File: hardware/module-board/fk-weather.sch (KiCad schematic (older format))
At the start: 66 parts, among them J1 MICRO-USB, J10 Conn_01x06, J11 Conn_01x06, J3 Conn_01x10, J6 CONN-HDR-2x5, M1 MOUNT_HOLE, M2 MOUNT_HOLE, M3 MOUNT_HOLE, M4 MOUNT_HOLE, Q1 2N7002LT1G, Q2 2N7002LT1G, Q3 2N7002LT1G, Q4 2N7002LT1G, SW1 SPNO, U1 ATSAMD21G18A-AU, U2 MCP1700T-XXX2E, U4 S25FL1xxK0XM, Y1 FC-135

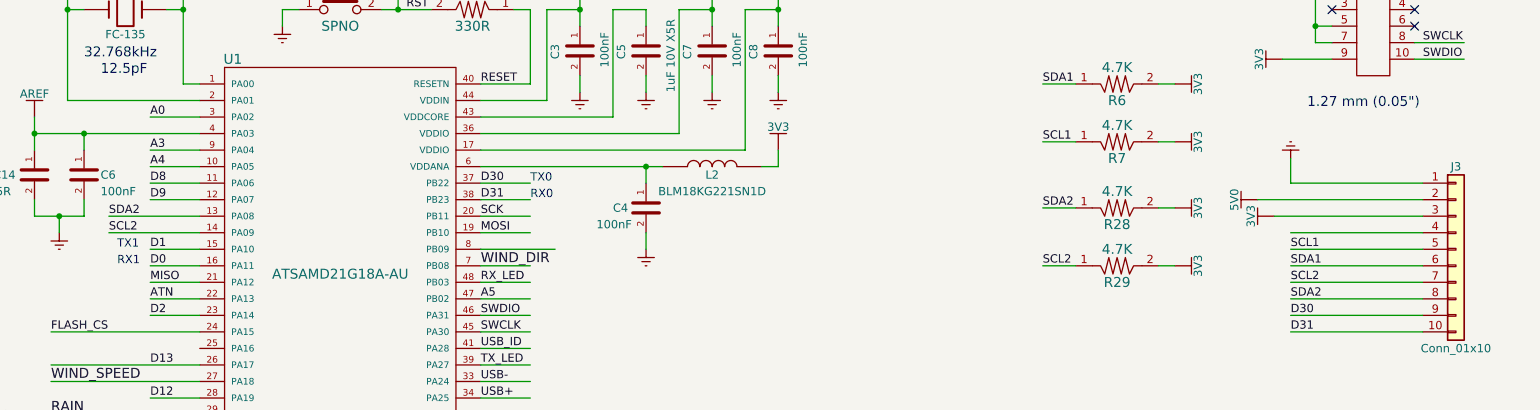
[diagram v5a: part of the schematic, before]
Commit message: Change header orien. Plot.
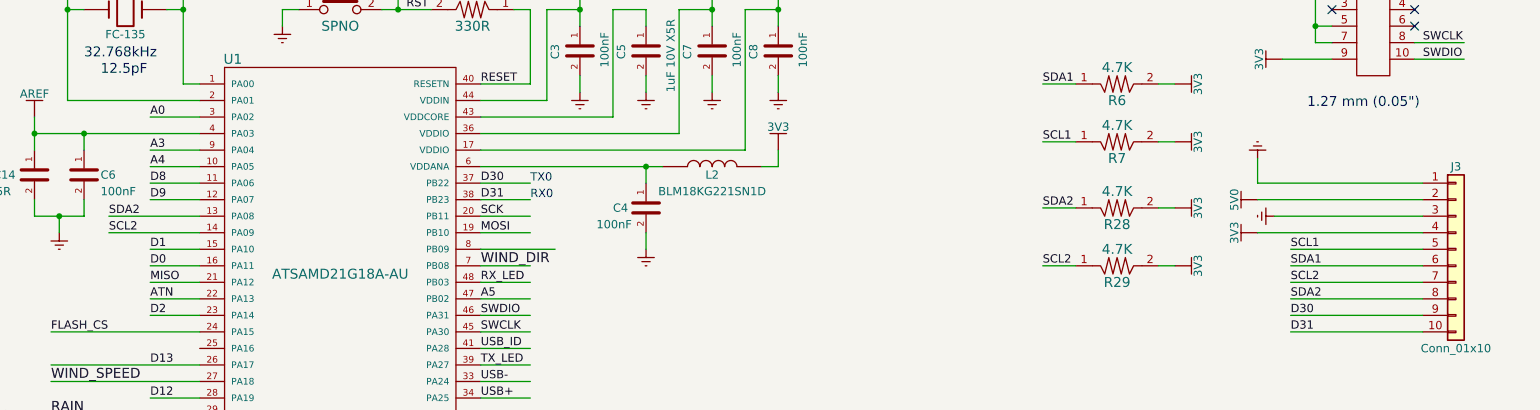
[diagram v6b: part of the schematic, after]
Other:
- note removed: "RX1"
- note removed: "TX1"
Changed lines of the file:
@@
 L 3V3 #PWR017
 U 1 1 5977AC6E
-P 9150 2750
-F 0 "#PWR017" H 9150 2600 50  0001 C CNN
-F 1 "3V3" H 9150 2890 50  0000 C CNN
-F 2 "" H 9150 2750 60  0000 C CNN
-F 3 "" H 9150 2750 60  0000 C CNN
-	1    9150 2750
+P 9050 2850
+F 0 "#PWR017" H 9050 2700 50  0001 C CNN
+F 1 "3V3" H 9050 2990 50  0000 C CNN
+F 2 "" H 9050 2850 60  0000 C CNN
+F 3 "" H 9050 2850 60  0000 C CNN
+	1    9050 2850
 	0    -1   -1   0
 $EndComp
@@
 L GND #PWR018
 U 1 1 5977ACB8
-P 9250 2400
-F 0 "#PWR018" H 9250 2150 50  0001 C CNN
-F 1 "GND" H 9250 2250 50  0001 C CNN
-F 2 "" H 9250 2400 60  0000 C CNN
-F 3 "" H 9250 2400 60  0000 C CNN
-	1    9250 2400
+P 9050 2400
+F 0 "#PWR018" H 9050 2150 50  0001 C CNN
+F 1 "GND" H 9050 2250 50  0001 C CNN
+F 2 "" H 9050 2400 60  0000 C CNN
+F 3 "" H 9050 2400 60  0000 C CNN
+	1    9050 2400
 	-1   0    0    1
 $EndComp
@@
 Text Notes 4650 2650 0    50   ~ 0
 RX0
-Text Notes 2150 3050 0    50   ~ 0
-RX1
-Text Notes 2150 2950 0    50   ~ 0
-TX1
 Text Notes 1100 4300 0    60   ~ 0
 M2.5 size
@@
 	4350 2450 5450 2450
 Wire Wire Line
-	9250 2850 10050 2850
+	9050 2850 10050 2850
 Wire Wire Line
 	9250 2950 10050 2950
@@
 	9150 2750 10050 2750
 Wire Wire Line
-	9250 2550 10050 2550
-Wire Wire Line
-	9250 2400 9250 2550
+	9050 2550 10050 2550
+Wire Wire Line
+	9050 2400 9050 2550
 Wire Wire Line
 	9050 2650 10050 2650
@@
 Wire Wire Line
 	9250 3450 10050 3450
+$Comp
+L GND #PWR051
+U 1 1 5A45CD21
+P 9150 2750
+F 0 "#PWR051" H 9150 2500 50  0001 C CNN
+F 1 "GND" H 9150 2600 50  0001 C CNN
+F 2 "" H 9150 2750 60  0000 C CNN
+F 3 "" H 9150 2750 60  0000 C CNN
+	1    9150 2750
+	0    1    1    0
+$EndComp
 $EndSCHEMATC

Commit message: Using the prettier footprints for some passives.
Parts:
- C1, C10, C11, C12, C14, C18, C2, C3, C4, C5, C6, C7, C8, C9: footprint Capacitors_SMD:C_0603_HandSoldering -> RocketScreamKicadLibrary:CAP-0603
- L1, L2: footprint Inductors_SMD:L_0603_HandSoldering -> RocketScreamKicadLibrary:IND-0603
- R1, R10, R17, R2, R22, R23, R28, R29, R3, R30, R31, R32, R33, R34, R4, R5, R6, R7, R8, R9: footprint Resistors_SMD:R_0603_HandSoldering -> RocketScreamKicadLibrary:RES-0603

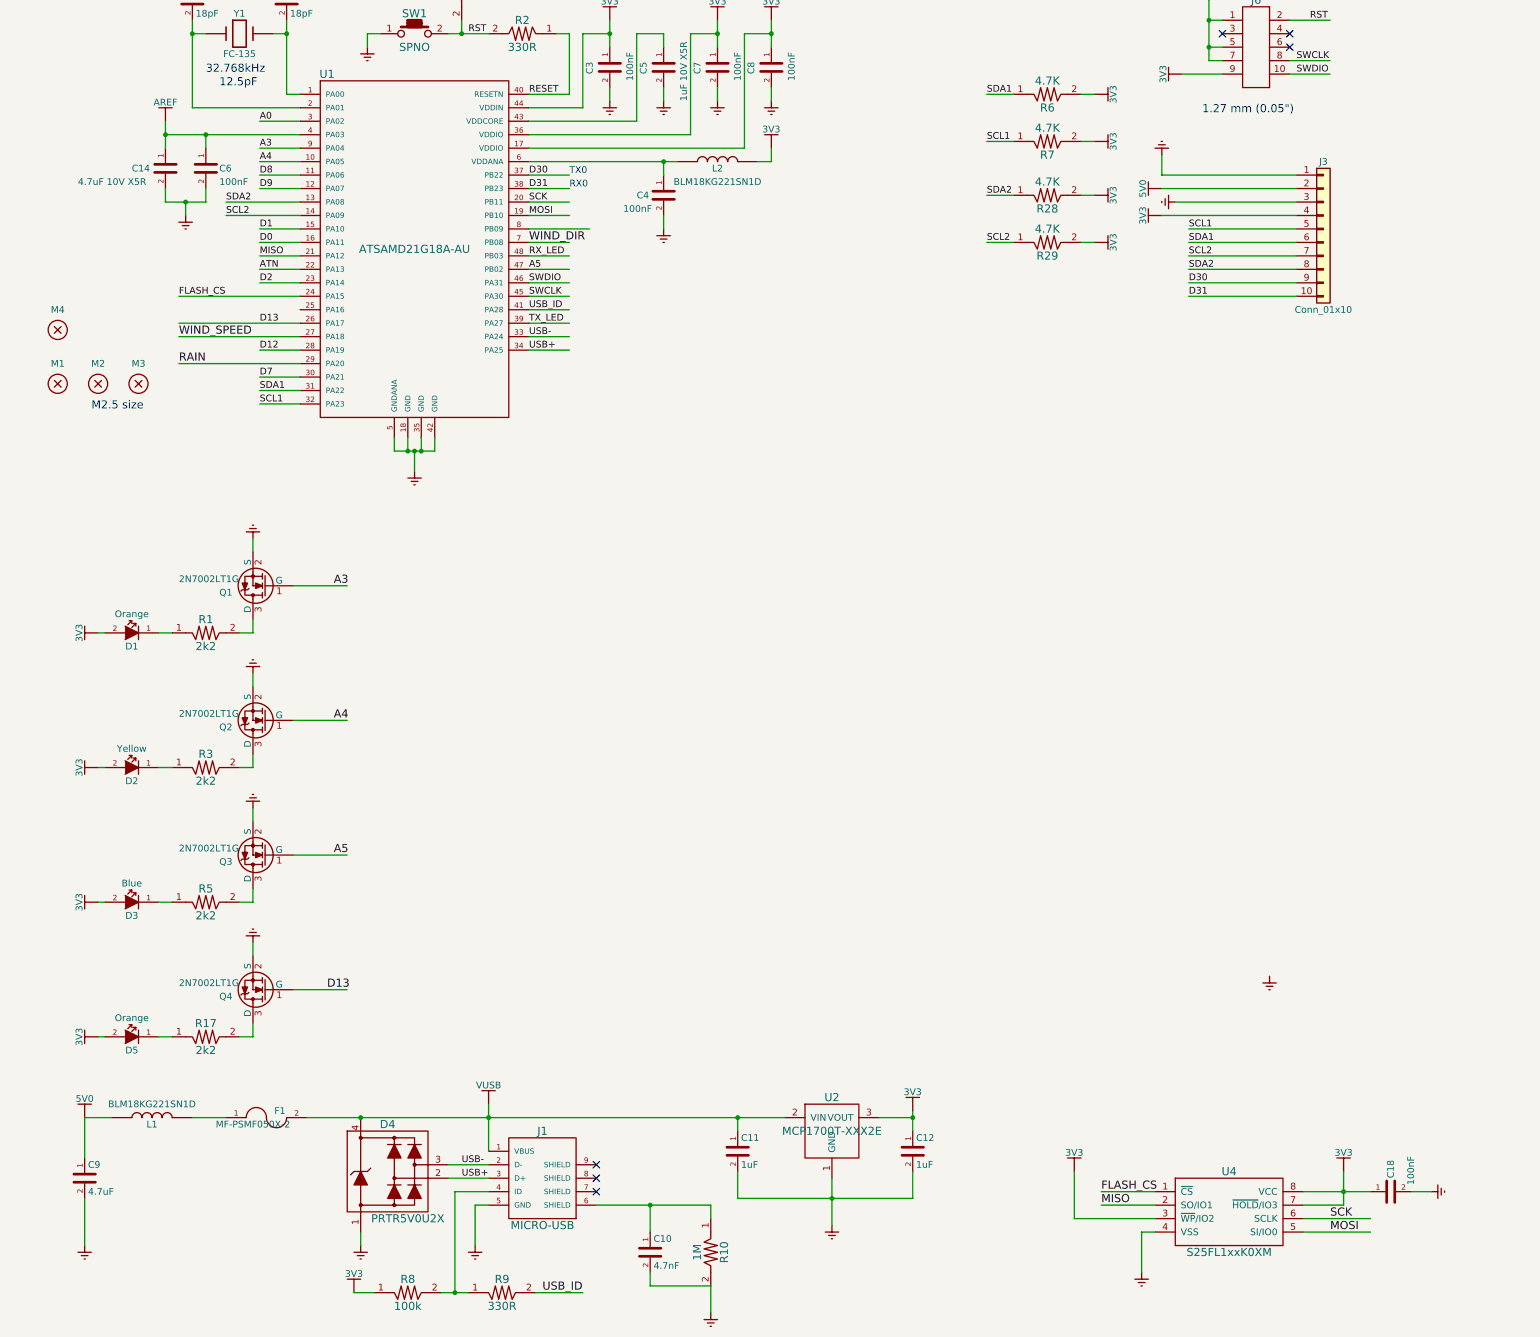
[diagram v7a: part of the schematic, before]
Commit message: Add NFET for peripherals. In this case just the flash.
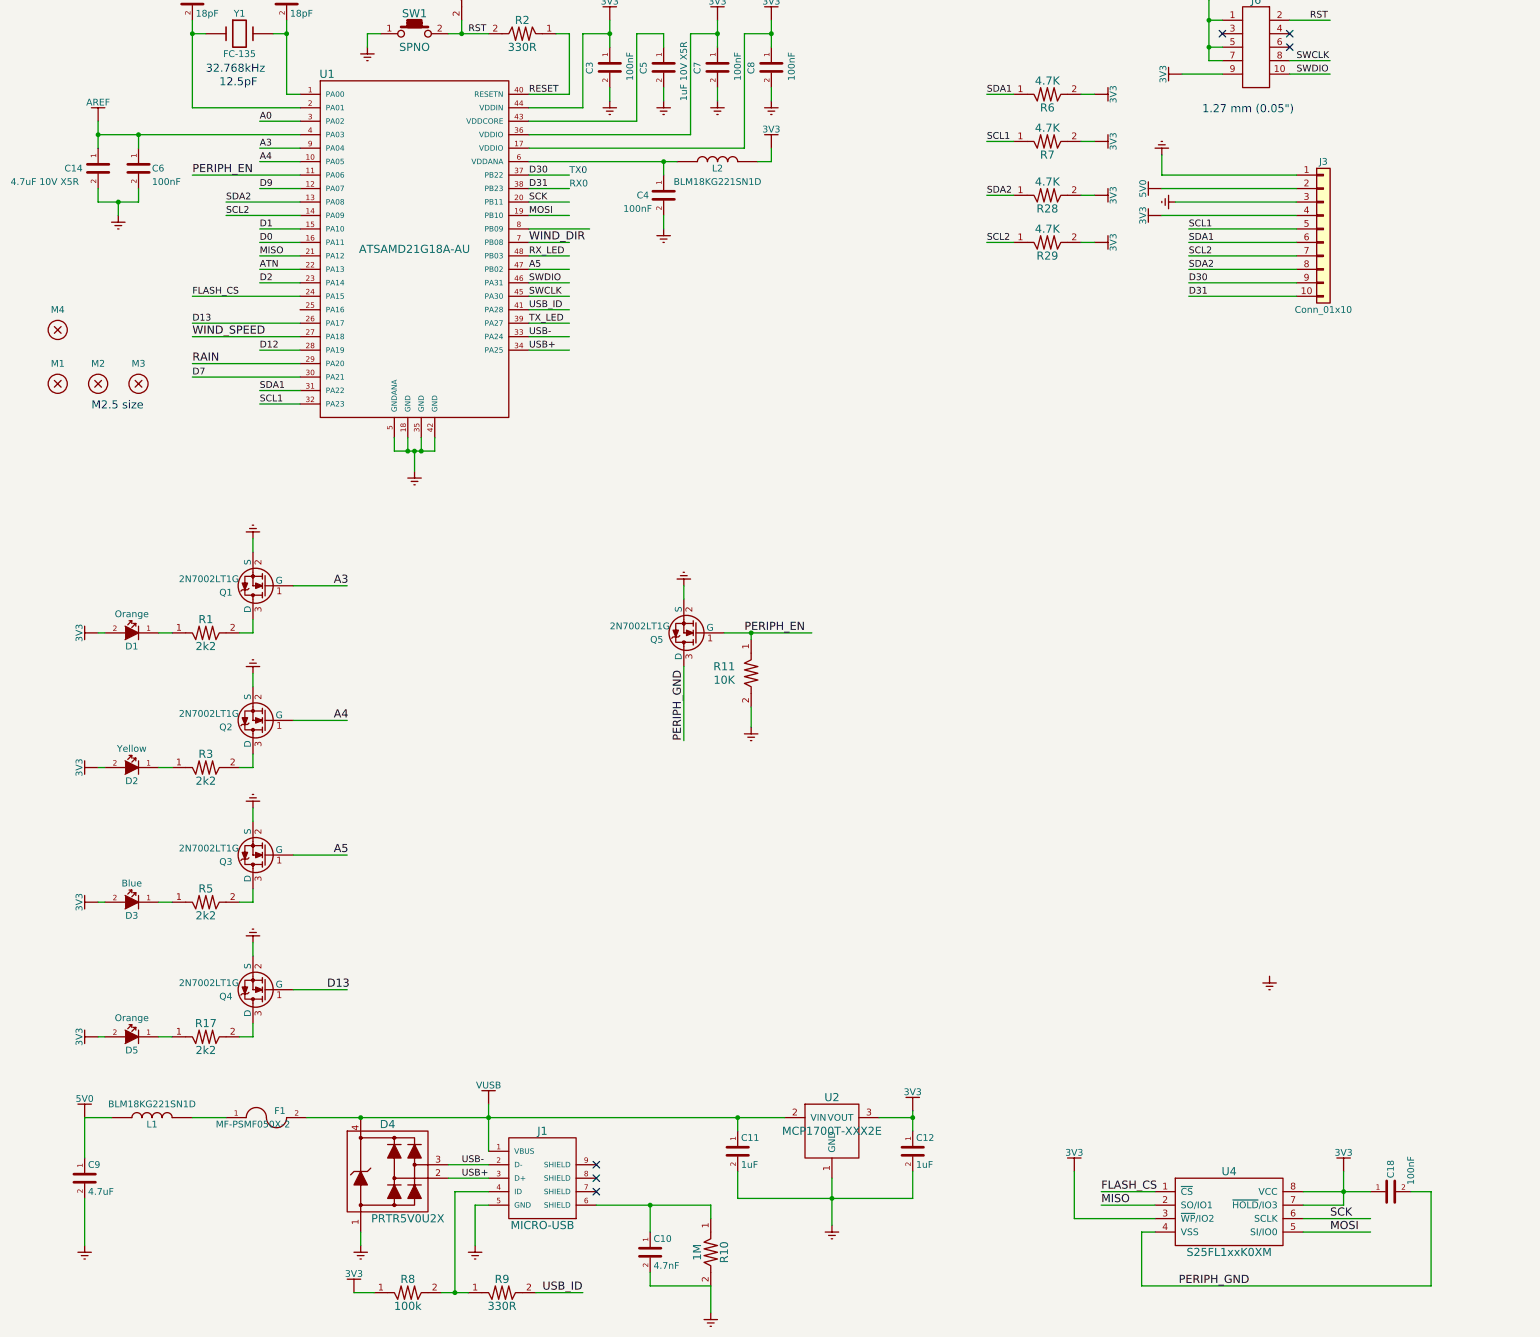
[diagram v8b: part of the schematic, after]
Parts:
- added Q5: 2N7002LT1G, RocketScreamKicadLibrary:SOT-23, symbol MOSFET-N
- added R11: 10K, RocketScreamKicadLibrary:RES-0603, symbol RESISTOR
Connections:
- net labels added: PERIPH_EN, PERIPH_GND
- net labels removed: D8
- wire segments 216 -> 223
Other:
- moved on the sheet: C14, C6
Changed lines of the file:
@@
 L AREF #PWR013
 U 1 1 56101489
-P 1650 2150
-F 0 "#PWR013" H 1650 2000 50  0001 C CNN
-F 1 "AREF" H 1650 2290 50  0000 C CNN
-F 2 "" H 1650 2150 60  0000 C CNN
-F 3 "" H 1650 2150 60  0000 C CNN
-	1    1650 2150
+P 1150 2150
+F 0 "#PWR013" H 1150 2000 50  0001 C CNN
+F 1 "AREF" H 1150 2290 50  0000 C CNN
+F 2 "" H 1150 2150 60  0000 C CNN
+F 3 "" H 1150 2150 60  0000 C CNN
+	1    1150 2150
 	1    0    0    -1
 $EndComp
@@
 L CAPACITOR-CERAMIC C6
 U 1 1 56101EA7
-P 1950 2500
-F 0 "C6" H 2050 2500 50  0000 L CNN
-F 1 "100nF" H 2050 2400 50  0000 L CNN
-F 2 "RocketScreamKicadLibrary:CAP-0603" H 1950 2300 30  0001 C CNN
-F 3 "" H 1950 2500 60  0000 C CNN
-F 4 "0" H 2050 2600 50  0001 C CNN "price"
-F 5 "81-GRM39X104K50D" H -200 -150 50  0001 C CNN "spn1"
-F 6 "mouser" H -200 -150 50  0001 C CNN "supplier1"
-	1    1950 2500
+P 1450 2500
+F 0 "C6" H 1550 2500 50  0000 L CNN
+F 1 "100nF" H 1550 2400 50  0000 L CNN
+F 2 "RocketScreamKicadLibrary:CAP-0603" H 1450 2300 30  0001 C CNN
+F 3 "" H 1450 2500 60  0000 C CNN
+F 4 "0" H 1550 2600 50  0001 C CNN "price"
+F 5 "81-GRM39X104K50D" H -700 -150 50  0001 C CNN "spn1"
+F 6 "mouser" H -700 -150 50  0001 C CNN "supplier1"
+	1    1450 2500
 	1    0    0    -1
 $EndComp
@@
 L CAPACITOR-CERAMIC C14
 U 1 1 561023B1
-P 1650 2500
-F 0 "C14" H 1400 2500 50  0000 L CNN
-F 1 "4.7uF 10V X5R" H 1000 2400 50  0000 L CNN
-F 2 "RocketScreamKicadLibrary:CAP-0603" H 1650 2300 30  0001 C CNN
-F 3 "" H 1650 2500 60  0000 C CNN
-F 4 "0" H 1400 2600 50  0001 C CNN "price"
-F 5 "581-0603ZD475MAT2A" H -200 -150 50  0001 C CNN "spn1"
-F 6 "mouser" H -200 -150 50  0001 C CNN "supplier1"
-	1    1650 2500
+P 1150 2500
+F 0 "C14" H 900 2500 50  0000 L CNN
+F 1 "4.7uF 10V X5R" H 500 2400 50  0000 L CNN
+F 2 "RocketScreamKicadLibrary:CAP-0603" H 1150 2300 30  0001 C CNN
+F 3 "" H 1150 2500 60  0000 C CNN
+F 4 "0" H 900 2600 50  0001 C CNN "price"
+F 5 "581-0603ZD475MAT2A" H -700 -150 50  0001 C CNN "spn1"
+F 6 "mouser" H -700 -150 50  0001 C CNN "supplier1"
+	1    1150 2500
 	1    0    0    -1
 $EndComp
@@
 L GND #PWR014
 U 1 1 5610322B
-P 1800 2850
-F 0 "#PWR014" H 1800 2600 50  0001 C CNN
-F 1 "GND" H 1800 2700 50  0001 C CNN
-F 2 "" H 1800 2850 60  0000 C CNN
-F 3 "" H 1800 2850 60  0000 C CNN
-	1    1800 2850
+P 1300 2850
+F 0 "#PWR014" H 1300 2600 50  0001 C CNN
+F 1 "GND" H 1300 2700 50  0001 C CNN
+F 2 "" H 1300 2850 60  0000 C CNN
+F 3 "" H 1300 2850 60  0000 C CNN
+	1    1300 2850
 	1    0    0    -1
 $EndComp
@@
 Text Label 2350 2450 0    50   ~ 0
 A4
-Text Label 2350 2550 0    50   ~ 0
-D8
 Text Label 2350 2650 0    50   ~ 0
 D9
@@
 Text Label 2350 3350 0    50   ~ 0
 D2
-Text Label 1750 3450 0    50   ~ 0
+Text Label 1850 3450 0    50   ~ 0
 FLASH_CS
 Text Label 2350 3850 0    50   ~ 0
 D12
-Text Label 2350 4050 0    50   ~ 0
-D7
 Text Label 2350 4150 0    50   ~ 0
 SDA1
@@
 Text Label 2850 8600 0    60   ~ 0
 D13
-Text Label 2350 3650 0    50   ~ 0
+Text Label 1850 3650 0    50   ~ 0
 D13
 Text Label 2100 2750 0    50   ~ 0
@@
 $EndComp
 $Comp
-L GND #PWR045
-U 1 1 5A1CDAB1
-P 11050 10100
-F 0 "#PWR045" H 11050 9850 50  0001 C CNN
-F 1 "GND" H 11050 9950 50  0001 C CNN
-F 2 "" H 11050 10100 60  0000 C CNN
-F 3 "" H 11050 10100 60  0000 C CNN
-	1    11050 10100
-	0    -1   -1   0
-$EndComp
-$Comp
 L Conn_01x06 J11
 U 1 1 5A44A535
@@
 	2650 2150 2350 2150
 Wire Wire Line
-	1650 2250 2650 2250
+	1150 2250 2650 2250
 Wire Wire Line
 	2650 2350 2350 2350
@@
 	2650 2450 2350 2450
 Wire Wire Line
-	2650 2550 2350 2550
+	1850 2550 2650 2550
 Wire Wire Line
 	2650 2650 2350 2650
@@
 	2650 3350 2350 3350
 Wire Wire Line
-	1750 3450 2650 3450
-Wire Wire Line
-	1750 3750 2650 3750
+	1850 3450 2650 3450
+Wire Wire Line
+	1850 3750 2650 3750
 Wire Wire Line
 	2650 3850 2350 3850
 Wire Wire Line
-	1750 3950 2650 3950
-Wire Wire Line
-	2650 4050 2350 4050
+	1850 3950 2650 3950
+Wire Wire Line
+	1850 4050 2650 4050
 Wire Wire Line
 	2650 4150 2350 4150
@@
 	1650 1000 1650 1100
 Wire Wire Line
-	1650 2150 1650 2350
-Wire Wire Line
 	4350 3850 4650 3850
 Wire Wire Line
@@
 	3850 800  3850 900
 Wire Wire Line
-	1950 2350 1950 2250
-Wire Wire Line
-	1650 2650 1650 2750
-Wire Wire Line
-	1650 2750 1950 2750
-Wire Wire Line
-	1950 2750 1950 2650
-Wire Wire Line
-	1800 2850 1800 2750
+	1150 2650 1150 2750
+Wire Wire Line
+	1150 2750 1450 2750
+Wire Wire Line
+	1450 2750 1450 2650
+Wire Wire Line
+	1300 2850 1300 2750
 Wire Wire Line
 	9400 1600 9500 1600
@@
 Connection ~ 5350 2450
 Connection ~ 3850 1500
-Connection ~ 1650 2250
-Connection ~ 1950 2250
-Connection ~ 1800 2750
+Connection ~ 1300 2750
 Connection ~ 9400 1600
 Connection ~ 3800 10850
@@
 	9000 10400 8900 10400
 Wire Wire Line
-	8900 10400 8900 10700
+	8900 10400 8900 10800
 Wire Wire Line
 	11050 10100 10900 10100
@@
 Connection ~ 14050 6350
 $Comp
-L 3V3 #PWR046
+L 3V3 #PWR045
 U 1 1 5A4678F1
 P 14500 4700
-F 0 "#PWR046" H 14500 4550 50  0001 C CNN
+F 0 "#PWR045" H 14500 4550 50  0001 C CNN
 F 1 "3V3" H 14500 4840 50  0000 C CNN
 F 2 "" H 14500 4700 60  0000 C CNN
@@
 Connection ~ 14500 4700
 $Comp
-L GND #PWR047
+L GND #PWR046
 U 1 1 5A46880E
 P 14600 6450
-F 0 "#PWR047" H 14600 6200 50  0001 C CNN
+F 0 "#PWR046" H 14600 6200 50  0001 C CNN
 F 1 "GND" H 14600 6300 50  0001 C CNN
 F 2 "" H 14600 6450 60  0000 C CNN
@@
 	14150 1850 14150 1750
 $Comp
-L 3V3 #PWR048
+L 3V3 #PWR047
 U 1 1 5A4762A6
 P 14150 1750
-F 0 "#PWR048" H 14150 1600 50  0001 C CNN
+F 0 "#PWR047" H 14150 1600 50  0001 C CNN
 F 1 "3V3" H 14150 1890 50  0000 C CNN
 F 2 "" H 14150 1750 60  0000 C CNN
@@
 $EndComp
 $Comp
-L GND #PWR049
+L GND #PWR048
 U 1 1 5A476B99
 P 14200 3350
-F 0 "#PWR049" H 14200 3100 50  0001 C CNN
+F 0 "#PWR048" H 14200 3100 50  0001 C CNN
 F 1 "GND" H 14200 3200 50  0001 C CNN
 F 2 "" H 14200 3350 60  0000 C CNN
@@
 Connection ~ 14200 3250
 Wire Wire Line
-	1750 3650 2650 3650
+	1850 3650 2650 3650
 Text Label 4350 3050 0    60   ~ 0
 WIND_DIR
-Text Label 1750 3750 0    60   ~ 0
+Text Label 1850 3750 0    60   ~ 0
 WIND_SPEED
-Text Label 1750 3950 0    60   ~ 0
+Text Label 1850 3950 0    60   ~ 0
 RAIN
 Text Label 9250 3250 0    50   ~ 0
@@
 Wire Wire Line
 	10050 3250 9250 3250
-$Comp
-L GND #PWR050
-U 1 1 5A46C08E
-P 8900 10700
-F 0 "#PWR050" H 8900 10450 50  0001 C CNN
-F 1 "GND" H 8900 10550 50  0001 C CNN
-F 2 "" H 8900 10700 60  0000 C CNN
-F 3 "" H 8900 10700 60  0000 C CNN
-	1    8900 10700
-	1    0    0    -1
-$EndComp
 $Comp
 L Conn_01x10 J3
@@
 	9250 3450 10050 3450
 $Comp
-L GND #PWR051
+L GND #PWR049
 U 1 1 5A45CD21
 P 9150 2750
-F 0 "#PWR051" H 9150 2500 50  0001 C CNN
+F 0 "#PWR049" H 9150 2500 50  0001 C CNN
 F 1 "GND" H 9150 2600 50  0001 C CNN
 F 2 "" H 9150 2750 60  0000 C CNN
@@
 	0    1    1    0
 $EndComp
+$Comp
+L MOSFET-N Q5
+U 1 1 5AF0968C
+P 5500 5950
+F 0 "Q5" H 5750 6000 50  0000 R CNN
+F 1 "2N7002LT1G" H 6050 5900 50  0000 R CNN
+F 2 "RocketScreamKicadLibrary:SOT-23" H 5500 5650 29  0001 C CNN
+F 3 "" H 5400 5950 60  0000 C CNN
+F 4 "0" H 5750 6100 50  0001 C CNN "price"
+F 5 "863-2N7002LT1G" H -4250 -1400 50  0001 C CNN "spn1"
+F 6 "mouser" H -4250 -1400 50  0001 C CNN "supplier1"
+	1    5500 5950
+	-1   0    0    1
+$EndComp
+$Comp
+L RESISTOR R11
+U 1 1 5AF0A304
+P 6000 6250
+F 0 "R11" V 5950 6050 60  0000 C CNN
+F 1 "10K" V 6050 6050 60  0000 C CNN
+F 2 "RocketScreamKicadLibrary:RES-0603" H 6000 6050 60  0001 C CNN
+F 3 "" H 6000 6250 60  0000 C CNN
+F 4 "0" H 5950 6150 50  0001 C CNN "price"
+F 5 "603-RC0603FR-0710KL" H 1950 4950 50  0001 C CNN "spn1"
+F 6 "mouser" H 1950 4950 50  0001 C CNN "supplier1"
+	1    6000 6250
+	0    1    1    0
+$EndComp
+$Comp
+L GND #PWR050
+U 1 1 5AF0A96F
+P 5500 5600
+F 0 "#PWR050" H 5500 5350 50  0001 C CNN
+F 1 "GND" H 5500 5450 50  0001 C CNN
+F 2 "" H 5500 5600 60  0000 C CNN
+F 3 "" H 5500 5600 60  0000 C CNN
+	1    5500 5600
+	-1   0    0    1
+$EndComp
+Wire Wire Line
+	5500 5700 5500 5600
+Wire Wire Line
+	5800 5950 6450 5950
+Wire Wire Line
+	6000 5950 6000 6000
+$Comp
+L GND #PWR051
+U 1 1 5AF0AE1F
+P 6000 6650
+F 0 "#PWR051" H 6000 6400 50  0001 C CNN
+F 1 "GND" H 6000 6500 50  0001 C CNN
+F 2 "" H 6000 6650 60  0000 C CNN
+F 3 "" H 6000 6650 60  0000 C CNN
+	1    6000 6650
+	1    0    0    -1
+$EndComp
+Wire Wire Line
+	6000 6500 6000 6650
+Connection ~ 6000 5950
+Text Label 5950 5950 0    60   ~ 0
+PERIPH_EN
+Text Label 5500 6750 1    60   ~ 0
+PERIPH_GND
+Wire Wire Line
+	5500 6200 5500 6750
+Text Label 1850 2550 0    60   ~ 0
+PERIPH_EN
+Text Label 9700 10800 2    60   ~ 0
+PERIPH_GND
+Wire Wire Line
+	8900 10800 11050 10800
+Wire Wire Line
+	11050 10800 11050 10100
+Wire Wire Line
+	1150 2150 1150 2350
+Connection ~ 1150 2250
+Wire Wire Line
+	1450 2250 1450 2350
+Connection ~ 1450 2250
+Text Label 1850 4050 0    50   ~ 0
+D7
 $EndSCHEMATC
